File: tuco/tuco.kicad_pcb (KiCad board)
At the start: 2 copper layers, 117 x 63.5 mm, 23 parts, among them J3 TSM-108-01-F-DV, J4 S16B-XH-A, U1 Teensy4.1

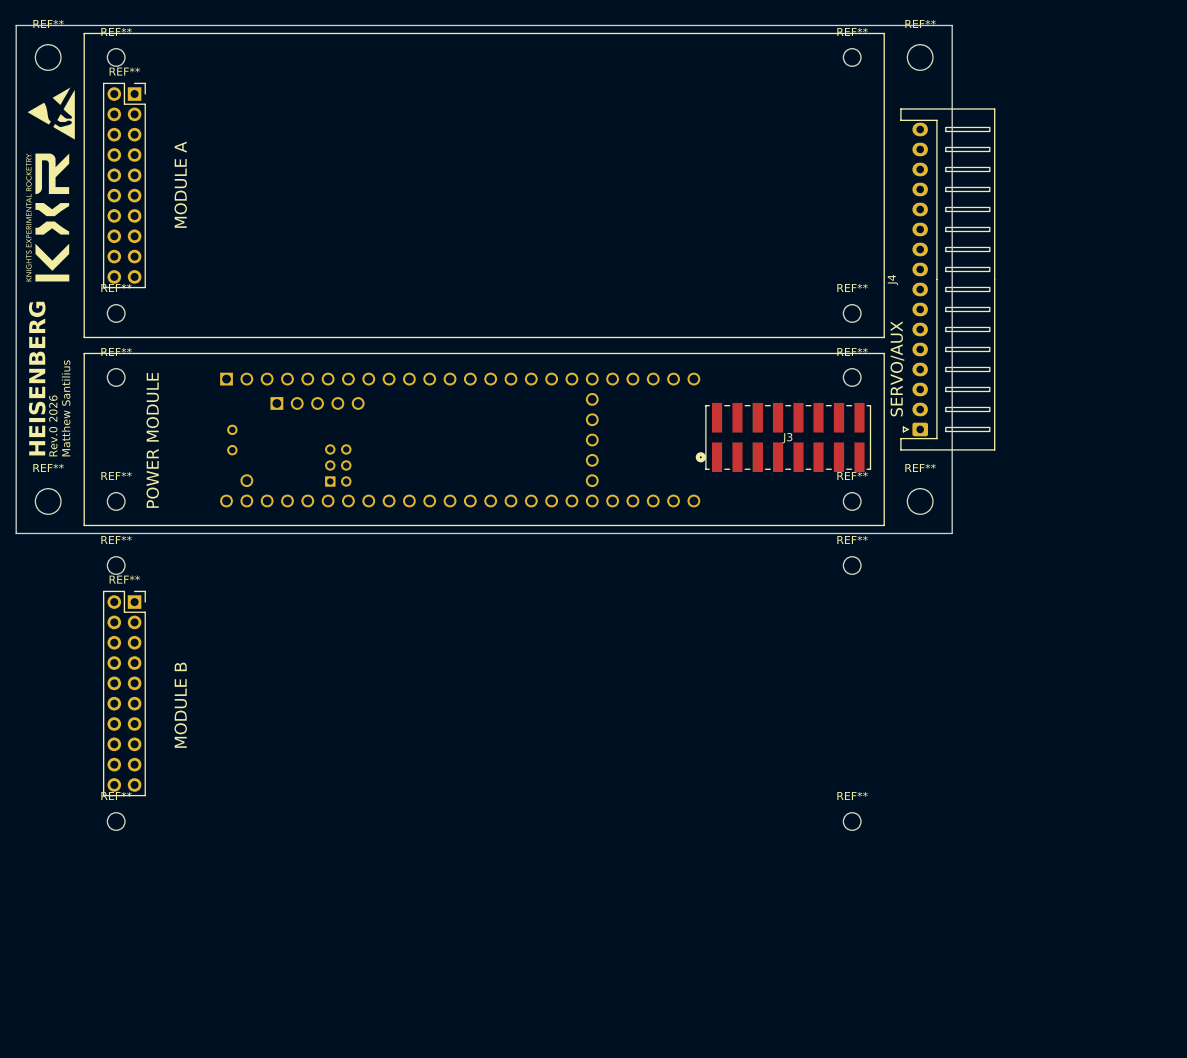
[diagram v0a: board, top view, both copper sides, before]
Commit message: Created Tuco board outline, heisenberg pin labels
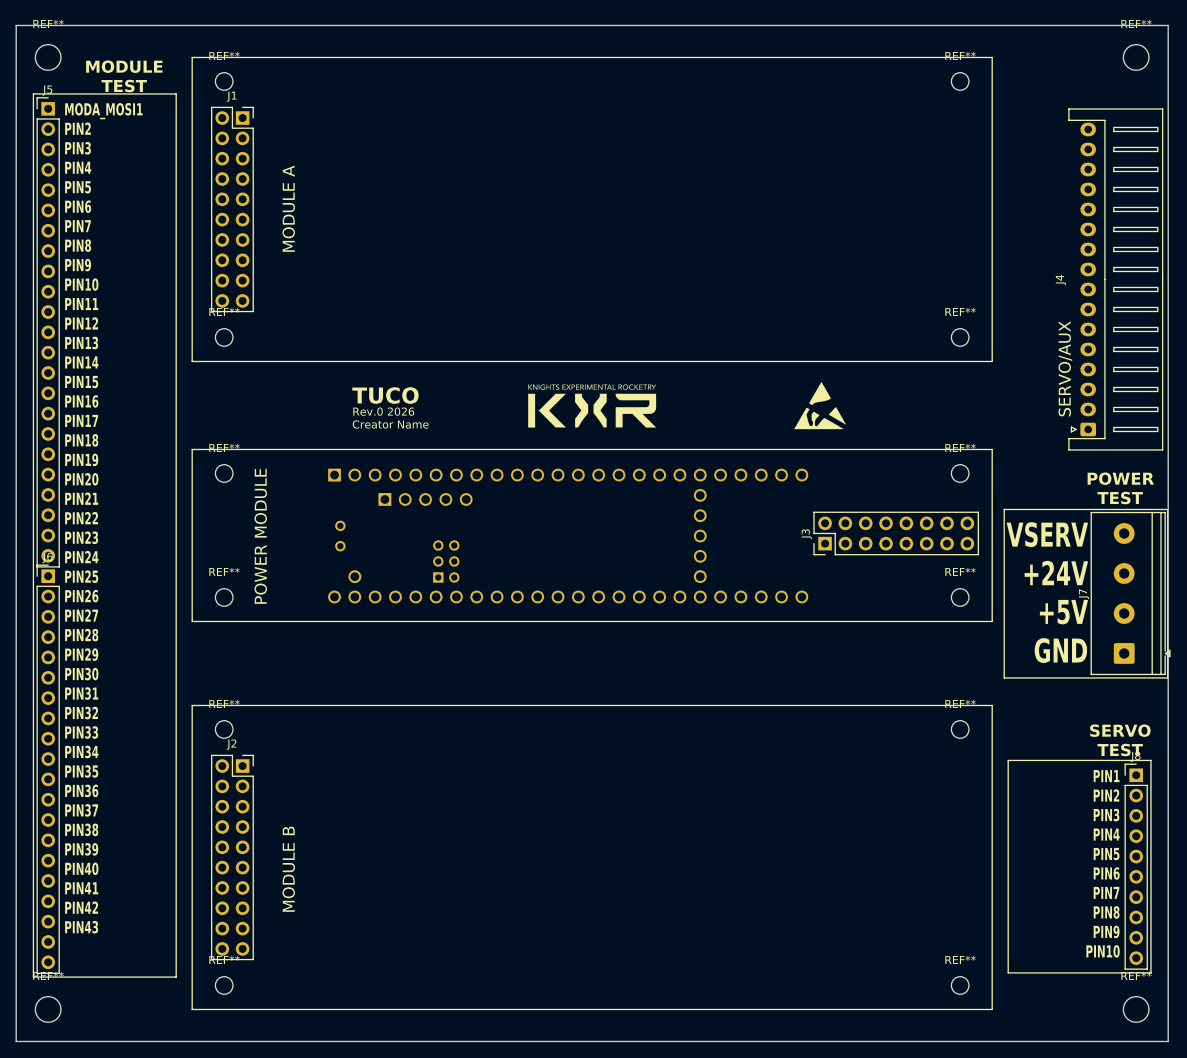
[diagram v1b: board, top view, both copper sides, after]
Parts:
- removed the REF** at (19.0, 74.5)
- removed the REF** at (29.8, 23.6)
- removed the REF** at (128.0, 74.5)
- removed the REF** at (29.8, 87.1)
- added J1: Conn_02x10_Odd_Even, Connector_PinSocket_2.54mm:PinSocket_2x10_P2.54mm_Vertical, F.Cu at (43.3, 26.6)
- added J2: Conn_02x10_Odd_Even, Connector_PinSocket_2.54mm:PinSocket_2x10_P2.54mm_Vertical, F.Cu at (43.3, 107.6)
- added J5: Conn_01x23, Connector_PinHeader_2.54mm:PinHeader_1x23_P2.54mm_Vertical, F.Cu at (19.0, 25.4)
- added J6: Conn_01x20, Connector_PinHeader_2.54mm:PinHeader_1x20_P2.54mm_Vertical, F.Cu at (19.0, 83.8)
- added J7: Screw_Terminal_01x04, TerminalBlock_Phoenix:TerminalBlock_Phoenix_PT-1,5-4-5.0-H_1x04_P5.00mm_Horizontal, F.Cu at (153.5, 93.5)
- added J8: Conn_01x10, Connector_PinHeader_2.54mm:PinHeader_1x10_P2.54mm_Vertical, F.Cu at (155.0, 108.7)
- added REF**: MountingHole_3.2mm_M3, MountingHole:MountingHole_3.2mm_M3, F.Cu at (155.0, 138.0)
- added REF**: MountingHole_3.2mm_M3, MountingHole:MountingHole_3.2mm_M3, F.Cu at (19.0, 138.0)
- J3: value TSM-108-01-F-DV -> Conn_01x16; footprint MDFC Common:CONN_TSM-108-01-F-DV_SAI -> Connector_PinHeader_2.54mm:PinHeader_2x08_P2.54mm_Vertical
- moved REF** 102.8 mm to (115.5, 62.5), turned to 0 degrees
- moved G*** 72.1 mm to (87.0, 62.5), turned to 0 degrees
- moved REF** 27.0 mm to (155.0, 19.0)
- moved REF** 24.5 mm to (41.0, 103.0)
- moved REF** 24.5 mm to (133.0, 135.0)
- moved REF** 24.5 mm to (133.0, 103.0)
- moved REF** 24.5 mm to (41.0, 135.0)
- moved J4 21.0 mm to (149.0, 65.5)
- moved REF** 18.1 mm to (41.0, 71.0)
- moved REF** 18.1 mm to (133.0, 71.0)
- moved REF** 18.1 mm to (41.0, 86.5)
- moved REF** 18.1 mm to (133.0, 86.5)
- moved U1 18.1 mm to (84.0, 78.8)
- moved J3 14.0 mm to (116.1, 79.8), turned to 90 degrees
- moved REF** 13.8 mm to (133.0, 54.0)
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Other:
- board size 117 x 63.5 mm -> 144 x 127 mm
- board text added: "MODA_MOSI1 PIN2 PIN3 PIN4 PIN5 PIN6 PIN7 PIN8 PIN9 PIN10 PIN11 PIN12 PIN13 PIN14 PIN15 PIN16 PIN17 PIN18 PIN19 PIN20 PIN21 PIN22 PIN23 PIN24 PIN25 PIN26 PIN27 PIN28 PIN29 PIN30 PIN31 PIN32 PIN33 PIN34 PIN35 PIN36 PIN37 PIN38 PIN39 PIN40 PIN41 PIN42 PIN43"
- board text added: "MODULE TEST"
- board text added: "PIN1 PIN2 PIN3 PIN4 PIN5 PIN6 PIN7 PIN8 PIN9 PIN10"
- board text added: "POWER TEST"
- board text added: "Rev.0 2026 Creator Name"
- board text added: "SERVO TEST"
- board text added: "TUCO"
- board text added: "VSERV +24V +5V GND"
- board text removed: "HEISENBERG"
- board text removed: "Rev.0 2026 Matthew Santilius"

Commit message: TUCO: Added net labels, servo/power prelim pinouts
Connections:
- J1 pad 1: unconnected-(J1-Pin_1-Pad1) -> /MODA_NET1
- J1 pad 20: unconnected-(J1-Pin_20-Pad20) -> /MODA_NET20
- J2 pad 1: unconnected-(J2-Pin_1-Pad1) -> /MODB_NET1
- J2 pad 20: unconnected-(J2-Pin_20-Pad20) -> /MODB_NET20
- J3 pad 1: unconnected-(J3-Pin_1-Pad1) -> GND
- J3 pad 10: unconnected-(J3-Pin_10-Pad10) -> +24V
- J3 pad 11: unconnected-(J3-Pin_11-Pad11) -> GND
- J3 pad 12: unconnected-(J3-Pin_12-Pad12) -> +V_SERVO
- J3 pad 13: unconnected-(J3-Pin_13-Pad13) -> GND
- J3 pad 14: unconnected-(J3-Pin_14-Pad14) -> +V_SERVO
- J3 pad 15: unconnected-(J3-Pin_15-Pad15) -> GND
- J3 pad 16: unconnected-(J3-Pin_16-Pad16) -> +V_SERVO
- J3 pad 2: unconnected-(J3-Pin_2-Pad2) -> GND
- J3 pad 3: unconnected-(J3-Pin_3-Pad3) -> +5V
- J3 pad 4: unconnected-(J3-Pin_4-Pad4) -> +5V
- J3 pad 5: unconnected-(J3-Pin_5-Pad5) -> /DIGI_PMOD_GPIO
- J3 pad 6: unconnected-(J3-Pin_6-Pad6) -> /I2C_PMOD_SDA
- J3 pad 7: unconnected-(J3-Pin_7-Pad7) -> /CAN_PMOD_TX
- J3 pad 8: unconnected-(J3-Pin_8-Pad8) -> /I2C_PMOD_SCL
- J3 pad 9: unconnected-(J3-Pin_9-Pad9) -> /CAN_PMOD_RX
- J4 pad 1: unconnected-(J4-Pad1) -> +V_SERVO
- J4 pad 10: unconnected-(J4-Pad10) -> /DIGI_SERVO_PWM1_H
- J4 pad 11: unconnected-(J4-Pad11) -> /DIGI_SERVO_PWM2_H
- J4 pad 12: unconnected-(J4-Pad12) -> /DIGI_SERVO_PWM3_H
- J4 pad 13: unconnected-(J4-Pad13) -> /DIGI_SERVO_PWM4_H
- J4 pad 14: unconnected-(J4-Pad14) -> /DIGI_SERVO_PWM5_H
- J4 pad 15: unconnected-(J4-Pad15) -> GND
- J4 pad 16: unconnected-(J4-Pad16) -> +5V
- J4 pad 2: unconnected-(J4-Pad2) -> +V_SERVO
- J4 pad 3: unconnected-(J4-Pad3) -> GND
- J4 pad 4: unconnected-(J4-Pad4) -> +V_SERVO
- J4 pad 5: unconnected-(J4-Pad5) -> GND
- J4 pad 6: unconnected-(J4-Pad6) -> /CAN_SERVO_TX
- J4 pad 7: unconnected-(J4-Pad7) -> /CAN_SERVO_RX
- J4 pad 8: unconnected-(J4-Pad8) -> /UART_SERVO_TX
- J4 pad 9: unconnected-(J4-Pad9) -> /UART_SERVO_RX
- J5 pad 1: unconnected-(J5-Pin_1-Pad1) -> /MODA_NET1
- J5 pad 20: unconnected-(J5-Pin_20-Pad20) -> /MODA_NET20
- J6 pad 1: unconnected-(J6-Pin_1-Pad1) -> /MODB_NET1
- J6 pad 20: unconnected-(J6-Pin_20-Pad20) -> /MODB_NET20
- J7 pad 1: unconnected-(J7-Pin_1-Pad1) -> +5V
- J7 pad 2: unconnected-(J7-Pin_2-Pad2) -> GND
- J7 pad 3: unconnected-(J7-Pin_3-Pad3) -> +24V
- J7 pad 4: unconnected-(J7-Pin_4-Pad4) -> +V_SERVO
- J8 pad 1: unconnected-(J8-Pin_1-Pad1) -> /CAN_SERVO_TX
- J8 pad 10: unconnected-(J8-Pin_10-Pad10) -> GND
- J8 pad 2: unconnected-(J8-Pin_2-Pad2) -> /CAN_SERVO_RX
- J8 pad 3: unconnected-(J8-Pin_3-Pad3) -> /UART_SERVO_TX
- J8 pad 4: unconnected-(J8-Pin_4-Pad4) -> /UART_SERVO_RX
- J8 pad 5: unconnected-(J8-Pin_5-Pad5) -> /DIGI_SERVO_PWM1_H
- J8 pad 6: unconnected-(J8-Pin_6-Pad6) -> /DIGI_SERVO_PWM2_H
- J8 pad 7: unconnected-(J8-Pin_7-Pad7) -> /DIGI_SERVO_PWM3_H
- J8 pad 8: unconnected-(J8-Pin_8-Pad8) -> /DIGI_SERVO_PWM4_H
- J8 pad 9: unconnected-(J8-Pin_9-Pad9) -> /DIGI_SERVO_PWM5_H
- U1 pad 1: unconnected-(U1-GND-Pad1) -> GND
- U1 pad 10: unconnected-(U1-8_TX2_IN1-Pad10) -> /UART_SERVO_TX
- U1 pad 11: unconnected-(U1-9_OUT1C-Pad11) -> /DIGI_MODA_PWM_H
- U1 pad 12: unconnected-(U1-10_CS_MQSR-Pad12) -> /SPI_MODB_CS
- U1 pad 13: unconnected-(U1-11_MOSI_CTX1-Pad13) -> /SPI_MODA_MOSI
- U1 pad 14: unconnected-(U1-12_MISO_MQSL-Pad14) -> /SPI_MODA_MISO
- U1 pad 16: unconnected-(U1-24_A10_TX6_SCL2-Pad16) -> /I2C_PMOD_SCL
- U1 pad 17: unconnected-(U1-25_A11_RX6_SDA2-Pad17) -> /I2C_PMOD_SDA
- U1 pad 18: unconnected-(U1-26_A12_MOSI1-Pad18) -> /SPI_MODB_MOSI
- U1 pad 19: unconnected-(U1-27_A13_SCK1-Pad19) -> /SPI_MODB_SCK
- U1 pad 2: unconnected-(U1-0_RX1_CRX2_CS1-Pad2) -> /SPI_MODB_CS1
- U1 pad 20: unconnected-(U1-28_RX7-Pad20) -> /UART_MODA_RX
- U1 pad 21: unconnected-(U1-29_TX7-Pad21) -> /UART_MODA_TX
- U1 pad 22: unconnected-(U1-30_CRX3-Pad22) -> /CAN_SERVO_RX
- U1 pad 23: unconnected-(U1-31_CTX3-Pad23) -> /CAN_SERVO_TX
- U1 pad 24: unconnected-(U1-32_OUT1B-Pad24) -> /DIGI_PMOD_GPIO
- U1 pad 25: unconnected-(U1-33_MCLK2-Pad25) -> /DIGI_MODB_PWM_H
- U1 pad 26: unconnected-(U1-34_RX8-Pad26) -> /UART_MODB_RX8
- U1 pad 27: unconnected-(U1-35_TX8-Pad27) -> /UART_MODB_TX8
- U1 pad 28: unconnected-(U1-36_CS-Pad28) -> /SPI_MODA_CS36
- U1 pad 29: unconnected-(U1-37_CS-Pad29) -> /SPI_MODA_CS37
- U1 pad 3: unconnected-(U1-1_TX1_CTX2_MISO1-Pad3) -> /SPI_MODB_MISO1
- U1 pad 30: unconnected-(U1-38_CS1_IN1-Pad30) -> /ANA_MODA_A14
- U1 pad 31: unconnected-(U1-39_MISO1_OUT1A-Pad31) -> /ANA_MODA_A15
- U1 pad 32: unconnected-(U1-40_A16-Pad32) -> /ANA_MODB_A16
- U1 pad 33: unconnected-(U1-41_A17-Pad33) -> /ANA_MODB_A17
- U1 pad 34: unconnected-(U1-GND-Pad34) -> GND
- U1 pad 35: unconnected-(U1-13_SCK_LED-Pad35) -> /SPI_MODA_SCK
- U1 pad 36: unconnected-(U1-14_A0_TX3_SPDIF_OUT-Pad36) -> /UART_MODA_TX
- U1 pad 37: unconnected-(U1-15_A1_RX3_SPDIF_IN-Pad37) -> /UART_MODA_RX
- U1 pad 38: unconnected-(U1-16_A2_RX4_SCL1-Pad38) -> /I2C_MODB_SCL1
- U1 pad 39: unconnected-(U1-17_A3_TX4_SDA1-Pad39) -> /I2C_MODB_SDA1
- U1 pad 4: unconnected-(U1-2_OUT2-Pad4) -> /DIGI_SERVO_PWM5_H
- U1 pad 40: unconnected-(U1-18_A4_SDA-Pad40) -> /I2C_MODA_SDA
- U1 pad 41: unconnected-(U1-19_A5_SCL-Pad41) -> /I2C_MODA_SCL
- U1 pad 42: unconnected-(U1-20_A6_TX5_LRCLK1-Pad42) -> /UART_MODB_TX5
- U1 pad 43: unconnected-(U1-21_A7_RX5_BCLK1-Pad43) -> /UART_MODB_RX5
- U1 pad 44: unconnected-(U1-22_A8_CTX1-Pad44) -> /CAN_PMOD_TX
- U1 pad 45: unconnected-(U1-23_A9_CRX1_MCLK1-Pad45) -> /CAN_PMOD_RX
- U1 pad 47: unconnected-(U1-GND-Pad47) -> GND
- U1 pad 48: unconnected-(U1-VIN-Pad48) -> +5V
- U1 pad 5: unconnected-(U1-3_LRCLK2-Pad5) -> /DIGI_SERVO_PWM4_H
- U1 pad 6: unconnected-(U1-4_BCLK2-Pad6) -> /DIGI_SERVO_PWM3_H
- U1 pad 60: unconnected-(U1-R+-Pad60) -> /ENET_PMOD_RX_P
- U1 pad 61: unconnected-(U1-LED-Pad61) -> /ENET_PMOD_LED_H
- U1 pad 62: unconnected-(U1-T--Pad62) -> /ENET_PMOD_TX_N
- U1 pad 63: unconnected-(U1-T+-Pad63) -> /ENET_PMOD_TX_P
- U1 pad 64: unconnected-(U1-GND-Pad64) -> GND
- U1 pad 65: unconnected-(U1-R--Pad65) -> /ENET_PMOD_RX_N
- U1 pad 7: unconnected-(U1-5_IN2-Pad7) -> /DIGI_SERVO_PWM2_H
- U1 pad 8: unconnected-(U1-6_OUT1D-Pad8) -> /DIGI_SERVO_PWM1_H
- U1 pad 9: unconnected-(U1-7_RX2_OUT1A-Pad9) -> /UART_SERVO_RX
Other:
- board text added: "CAN_SERVO_TX CAN_SERVO_RX UART_SERVO_TX UART_SERVO_RX DIGI_SRV_PWM1 DIGI_SRV_PWM2 DIGI_SRV_PWM3 DIGI_SRV_PWM4 DIGI_SRV_PWM5 GROUND"
- board text added: "VSERV +24V GND +5V"
- board text removed: "PIN1 PIN2 PIN3 PIN4 PIN5 PIN6 PIN7 PIN8 PIN9 PIN10"
- board text removed: "VSERV +24V +5V GND"
